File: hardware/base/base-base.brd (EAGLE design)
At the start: 76.2 x 101.3 mm, 33 parts, among them T2 BC337, U1 SD_CARD_SOCKET2041021FFROMTES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, X1 BU-SMA-1-7HOLE

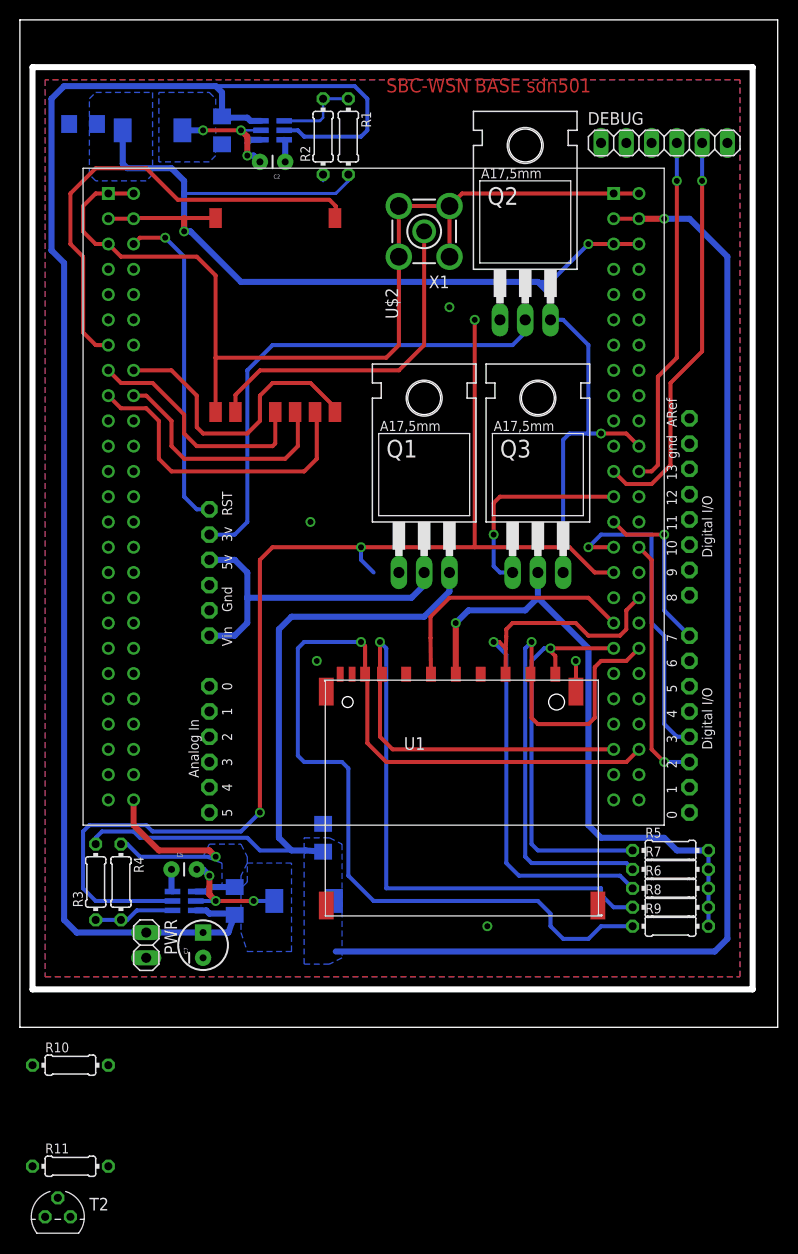
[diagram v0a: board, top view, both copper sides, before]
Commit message: Fixed bad transistor setup
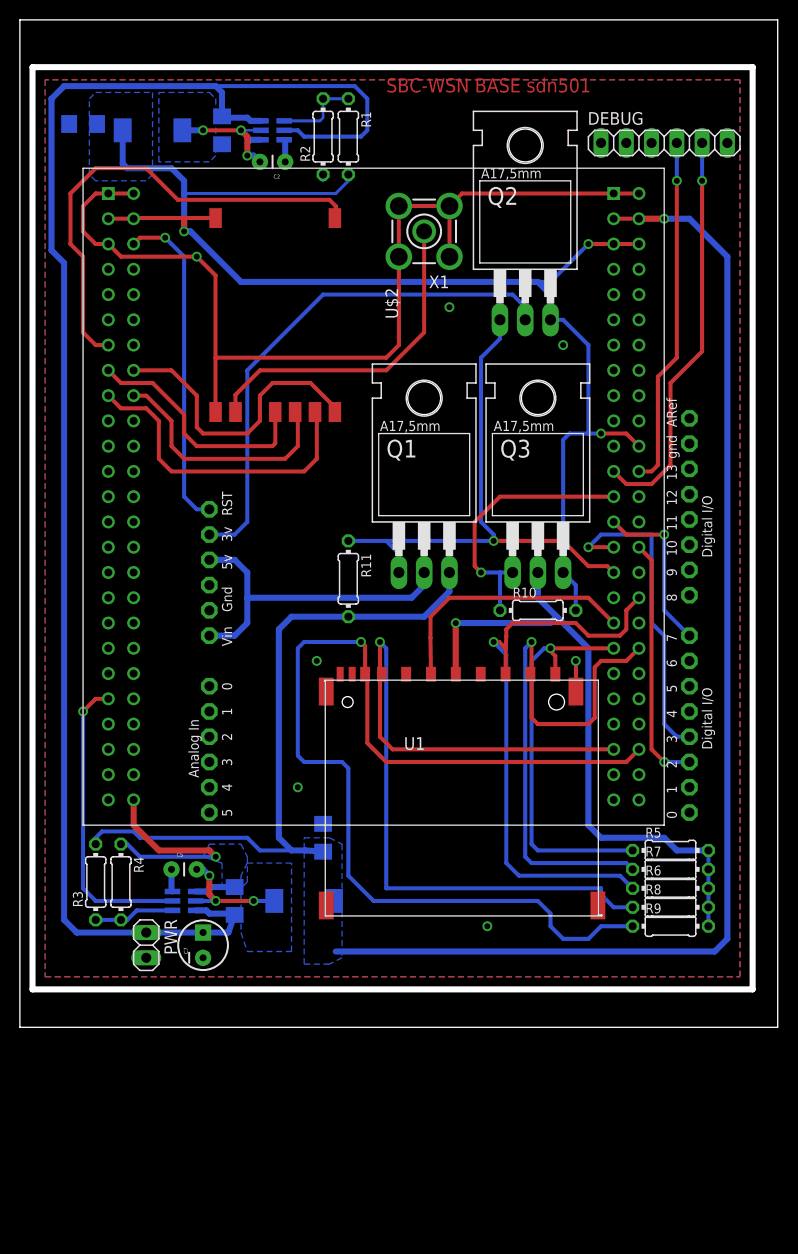
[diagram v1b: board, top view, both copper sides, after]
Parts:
- removed T2: BC337, transistor:TO92
- moved R10 65.6 mm to (52.1, 41.9)
- moved R11 65.3 mm to (33.0, 45.1), turned to 270 degrees
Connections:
- removed net GSM_TRANSISTORLINE: Q1.G, Q2.G, R11.1, T2.3
- new net 5V_RAIL_EN: U$1.P$41, U$5.5
- net GND: no longer T2.1
- net GSM_PWR: now also Q1.G, Q2.G, R11.1; no longer T2.2, U$5.5
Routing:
- net GSM_PWR: track 122.8 -> 55.2 mm, vias 3 -> 1
- net 5V_RAIL_EN: track 0.00 -> 30.4 mm, vias 0 -> 1
- net SD_PWR: track 20.8 -> 27.4 mm
- net +3V3: track 134.4 -> 138.8 mm
- net N$2: track 50.4 -> 52.5 mm
- net SD_VCC: track 62.9 -> 64.0 mm
- net RADIO_ANT: track 34.2 -> 33.5 mm
- net GND: vias 6 -> 8
